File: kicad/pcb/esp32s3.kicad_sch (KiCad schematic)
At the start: 7 parts, among them SW1 SW_Push, U3 ESP32-S3-WROOM-2, Y1 Crystal_GND23

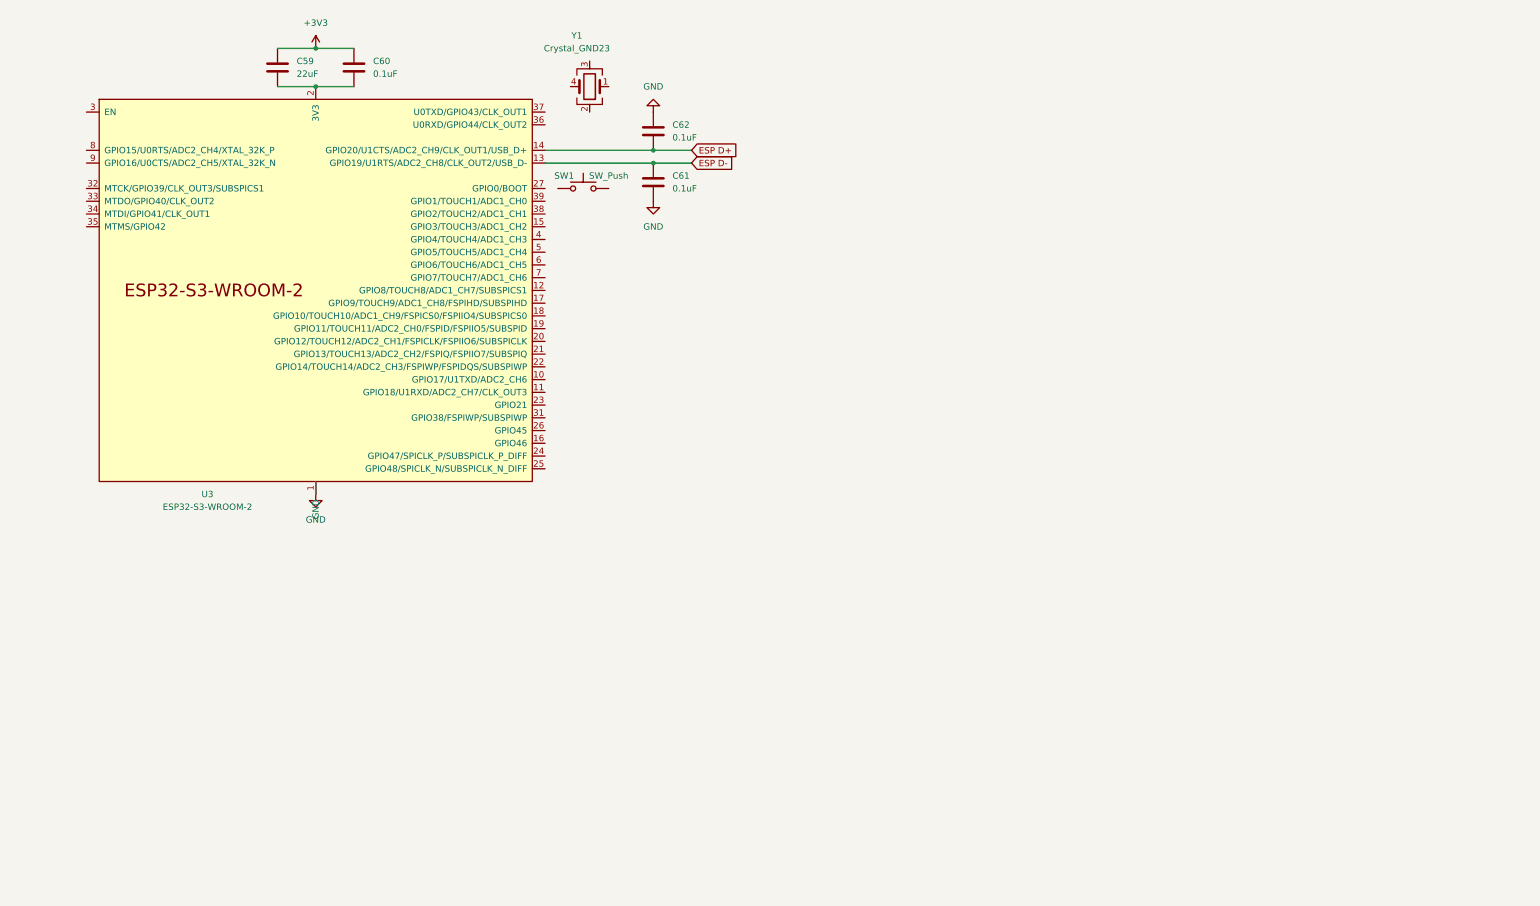
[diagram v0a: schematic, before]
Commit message: USB (almost) done + some STM progress
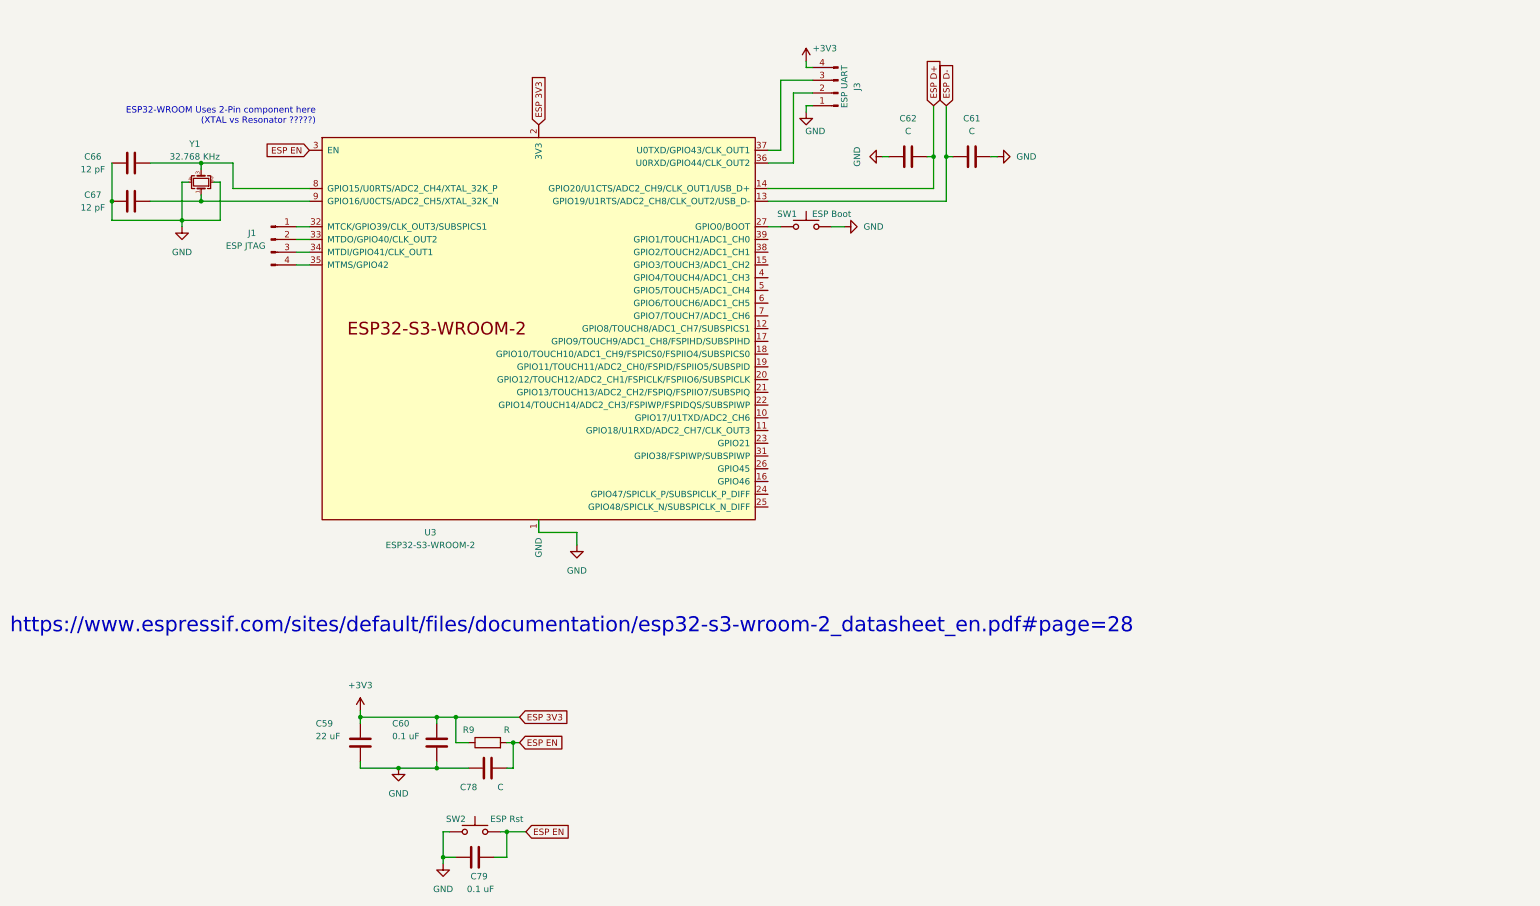
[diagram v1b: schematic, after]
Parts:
- removed Y1: Crystal_GND23, symbol Device:Crystal_GND23
- added C66, C67: 12 pF, symbol Device:C
- added C78: C, symbol Device:C
- added C79: 0.1 uF, symbol Device:C
- added J1: ESP JTAG, symbol Connector:Conn_01x04_Pin
- added J3: ESP UART, symbol Connector:Conn_01x04_Pin
- added R9: R, symbol Device:R
- added SW2: ESP Rst, symbol Switch:SW_Push
- added Y1: 32.768 KHz, symbol Device:Crystal_GND24_Small
- C59: value 22uF -> 22 uF
- C60: value 0.1uF -> 0.1 uF
- C61, C62: value 0.1uF -> C
- SW1: value SW_Push -> ESP Boot
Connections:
- net +3V3: now also U3.2 (3V3), J3.4 (Pin_4), R9.1
- net GND: now also C59.2, C60.2, SW1.2, C66.1, C67.2, C78.1, C79.1, J3.1 (Pin_1), SW2.1, Y1.2, Y1.4
- net at SW1.1: now also U3.27 (GPIO0/BOOT)
- net ESP EN: now reaches U3.3 (EN)
- net ESP EN: now also C78.2, C79.2, R9.2, SW2.2
- net at U3.32 (MTCK/GPIO39/CLK_OUT3/SUBSPICS1): now also J1.1 (Pin_1)
- net at U3.33 (MTDO/GPIO40/CLK_OUT2): now also J1.2 (Pin_2)
- net at U3.34 (MTDI/GPIO41/CLK_OUT1): now also J1.3 (Pin_3)
- net at U3.35 (MTMS/GPIO42): now also J1.4 (Pin_4)
- net at U3.36 (U0RXD/GPIO44/CLK_OUT2): now also J3.2 (Pin_2)
- net at U3.37 (U0TXD/GPIO43/CLK_OUT1): now also J3.3 (Pin_3)
- net at U3.8 (GPIO15/U0RTS/ADC2_CH4/XTAL_32K_P): now also C66.2, Y1.3
- net at U3.9 (GPIO16/U0CTS/ADC2_CH5/XTAL_32K_N): now also C67.1, Y1.1
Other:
- note added: "ESP32-WROOM Uses 2-Pin component here (XTAL vs Resonator ?????)"
- note added: "https://www.espressif.com/sites/default/files/documentation/esp32-s3-wroom-2_datasheet_en.pdf#page=28"
- moved on the sheet: C61, C62, SW1, U3

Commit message: Initial support circuitry for STM and ESP
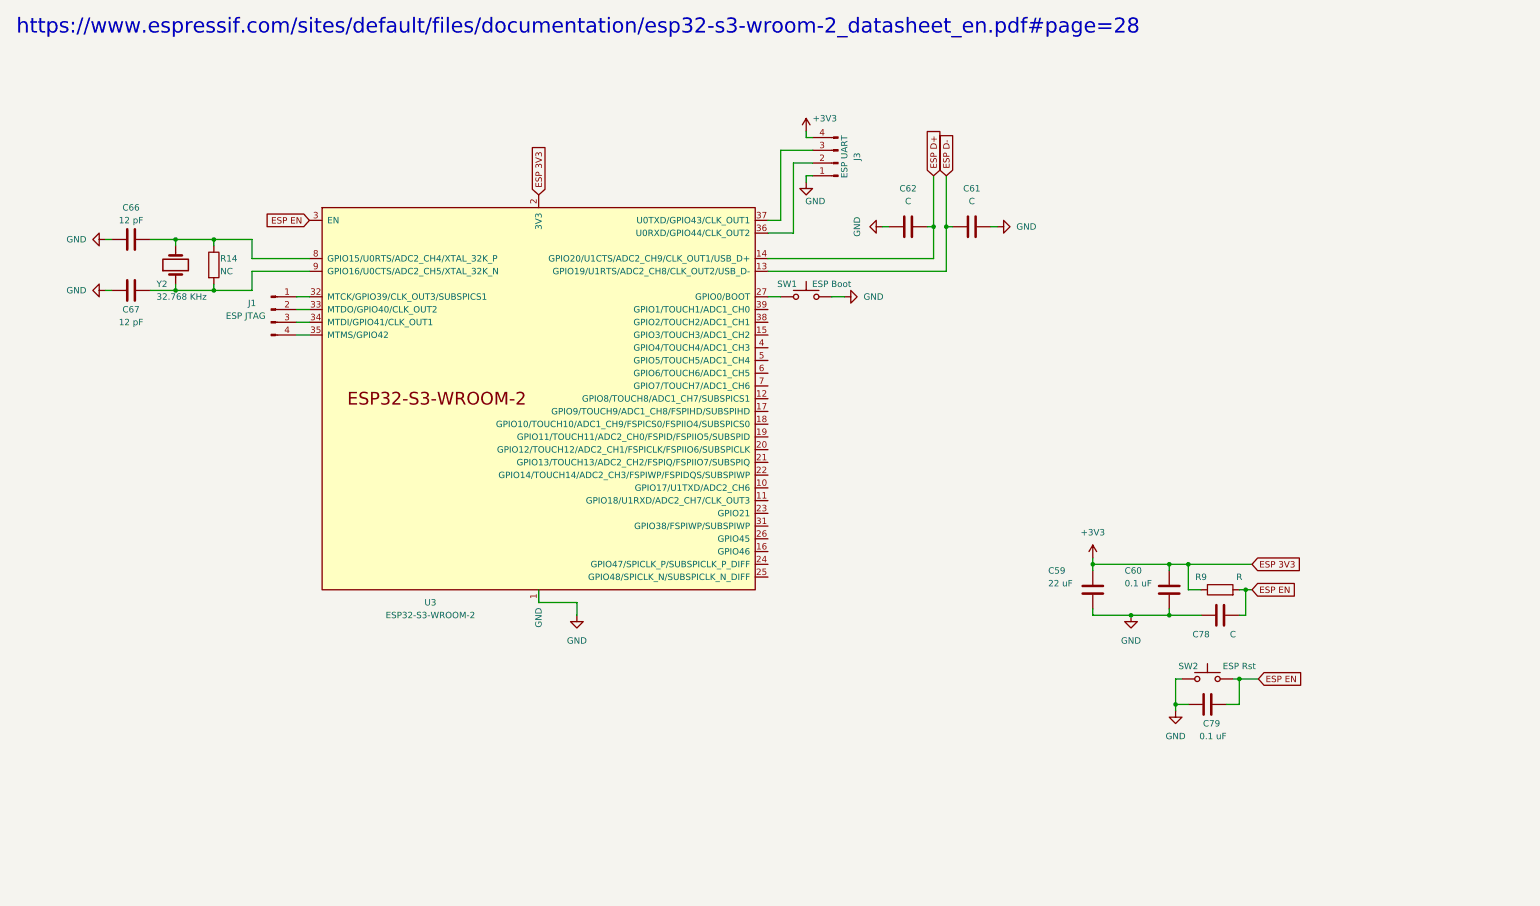
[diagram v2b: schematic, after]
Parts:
- removed Y1: 32.768 KHz, symbol Device:Crystal_GND24_Small
- added R14: NC, symbol Device:R
- added Y2: 32.768 KHz, symbol Device:Crystal
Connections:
- net at C67.1, U3.9 (GPIO16/U0CTS/ADC2_CH5/XTAL_32K_N): now also R14.2, Y2.1
- net at C66.2, U3.8 (GPIO15/U0RTS/ADC2_CH4/XTAL_32K_P): now also R14.1, Y2.2
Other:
- note removed: "ESP32-WROOM Uses 2-Pin component here (XTAL vs Resonator ?????)"
- moved on the sheet: C59, C60, C61, C62, C66, C67, C78, C79, J1, J3, R9, SW1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

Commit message: Initial wiring sorted out?
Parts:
- removed J1: ESP JTAG, symbol Connector:Conn_01x04_Pin
- removed J3: ESP UART, symbol Connector:Conn_01x04_Pin
- added J1: ESP JTAG, symbol Connector_Generic:Conn_01x04
- added J3: ESP UART, symbol Connector_Generic:Conn_01x04
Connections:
- net +3V3: now also J3.1 (Pin_1)
- net GND: now also J3.4 (Pin_4)
- net at U3.36 (U0RXD/GPIO44/CLK_OUT2): now also J3.3 (Pin_3)
- net at U3.37 (U0TXD/GPIO43/CLK_OUT1): now also J3.2 (Pin_2)
- net at U3.32 (MTCK/GPIO39/CLK_OUT3/SUBSPICS1): now also J1.4 (Pin_4)
- net at U3.33 (MTDO/GPIO40/CLK_OUT2): now also J1.3 (Pin_3)
- net at U3.34 (MTDI/GPIO41/CLK_OUT1): now also J1.2 (Pin_2)
- net at U3.35 (MTMS/GPIO42): now also J1.1 (Pin_1)
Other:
- moved on the sheet: C61, C62, C66, C67, R14, SW1, U3, Y2

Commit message: Hub wired(?) + STM and ESP may boot already
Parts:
- C59: value 22 uF -> 22u; footprint (none) -> Capacitor_SMD:C_0402_1005Metric_Pad0.74x0.62mm_HandSolder
- C60, C79: value 0.1 uF -> 0.1u; footprint (none) -> Capacitor_SMD:C_0402_1005Metric_Pad0.74x0.62mm_HandSolder
- C61, C62, C78: footprint (none) -> Capacitor_SMD:C_0402_1005Metric_Pad0.74x0.62mm_HandSolder
- C66, C67: value 12 pF -> 12p; footprint (none) -> Capacitor_SMD:C_0402_1005Metric_Pad0.74x0.62mm_HandSolder
- J1, J3: footprint (none) -> Connector_PinHeader_2.54mm:PinHeader_1x04_P2.54mm_Vertical_SMD_Pin1Right
- R14, R9: footprint (none) -> Resistor_SMD:R_0402_1005Metric_Pad0.72x0.64mm_HandSolder
- SW1, SW2: footprint (none) -> Button_Switch_SMD:SW_Push_1P1T_NO_CK_KMR2
- Y2: footprint (none) -> Crystal:Crystal_SMD_2012-2Pin_2.0x1.2mm
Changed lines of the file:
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@@
   (junction (at 266.7 129.54) (diameter 0) (color 0 0 0 0)
   )
-  (junction (at 255.27 124.46) (diameter 0) (color 0 0 0 0)
-  )
   (junction (at 243.84 134.62) (diameter 0) (color 0 0 0 0)
   )
@@
     (stroke (width 0) (type default))
   )
-  (wire (pts (xy 255.27 124.46) (xy 267.97 124.46))
-    (stroke (width 0) (type default))
-  )
   (wire (pts (xy 196.85 55.88) (xy 198.12 55.88))
     (stroke (width 0) (type default))
@@
   )
   (wire (pts (xy 151.13 148.59) (xy 143.51 148.59))
+    (stroke (width 0) (type default))
+  )
+  (wire (pts (xy 143.51 66.04) (xy 143.51 67.31))
     (stroke (width 0) (type default))
   )
@@
     )
   )
-  (global_label "ESP 3V3" (shape input) (at 143.51 67.31 90) (fields_autoplaced)
-    (effects (font (size 1.27 1.27)) (justify left))
-    (property "Intersheetrefs" "${INTERSHEET_REFS}" (at 143.51 56.2211 90)
-      (effects (font (size 1.27 1.27)) (justify left) hide)
-    )
-  )
   (global_label "ESP EN" (shape input) (at 267.97 129.54 0) (fields_autoplaced)
     (effects (font (size 1.27 1.27)) (justify left))
@@
     )
   )
-  (global_label "ESP 3V3" (shape input) (at 267.97 124.46 0) (fields_autoplaced)
-    (effects (font (size 1.27 1.27)) (justify left))
-    (property "Intersheetrefs" "${INTERSHEET_REFS}" (at 279.0589 124.46 0)
-      (effects (font (size 1.27 1.27)) (justify left) hide)
-    )
-  )
   (global_label "ESP D-" (shape input) (at 224.79 63.5 90) (fields_autoplaced)
     (effects (font (size 1.27 1.27)) (justify left))
@@
       (effects (font (size 1.27 1.27)) (justify left))
     )
-    (property "Footprint" "" (at 203.2 58.42 0)
+    (property "Footprint" "Connector_PinHeader_2.54mm:PinHeader_1x04_P2.54mm_Vertical_SMD_Pin1Right" (at 203.2 58.42 0)
       (effects (font (size 1.27 1.27)) hide)
     )
@@
       (effects (font (size 1.27 1.27)))
     )
-    (property "Footprint" "" (at 265.43 133.6548 0)
+    (property "Footprint" "Capacitor_SMD:C_0402_1005Metric_Pad0.74x0.62mm_HandSolder" (at 265.43 133.6548 0)
       (effects (font (size 1.27 1.27)) hide)
     )
@@
       (effects (font (size 1.27 1.27)))
     )
-    (property "Footprint" "" (at 196.85 82.55 0)
+    (property "Footprint" "Button_Switch_SMD:SW_Push_1P1T_NO_CK_KMR2" (at 196.85 82.55 0)
       (effects (font (size 1.27 1.27)) hide)
     )
@@
       (effects (font (size 1.27 1.27)) (justify right))
     )
-    (property "Footprint" "" (at 71.12 81.28 0)
+    (property "Footprint" "Crystal:Crystal_SMD_2012-2Pin_2.0x1.2mm" (at 71.12 81.28 0)
       (effects (font (size 1.27 1.27)) hide)
     )
@@
       (effects (font (size 1.27 1.27)))
     )
-    (property "Footprint" "" (at 261.62 131.318 90)
+    (property "Footprint" "Resistor_SMD:R_0402_1005Metric_Pad0.72x0.64mm_HandSolder" (at 261.62 131.318 90)
       (effects (font (size 1.27 1.27)) hide)
     )
@@
       (effects (font (size 1.27 1.27)) (justify left))
     )
-    (property "Value" "0.1 uF" (at 242.57 128.27 0)
-      (effects (font (size 1.27 1.27)) (justify left))
-    )
-    (property "Footprint" "" (at 252.4252 133.35 0)
+    (property "Value" "0.1u" (at 242.57 128.27 0)
+      (effects (font (size 1.27 1.27)) (justify left))
+    )
+    (property "Footprint" "Capacitor_SMD:C_0402_1005Metric_Pad0.74x0.62mm_HandSolder" (at 252.4252 133.35 0)
       (effects (font (size 1.27 1.27)) hide)
     )
@@
       (effects (font (size 1.27 1.27)))
     )
-    (property "Footprint" "" (at 213.36 74.6252 0)
+    (property "Footprint" "Capacitor_SMD:C_0402_1005Metric_Pad0.74x0.62mm_HandSolder" (at 213.36 74.6252 0)
       (effects (font (size 1.27 1.27)) hide)
     )
@@
       (effects (font (size 1.27 1.27)) (justify left))
     )
-    (property "Value" "22 uF" (at 227.33 128.27 0)
-      (effects (font (size 1.27 1.27)) (justify left))
-    )
-    (property "Footprint" "" (at 237.1852 133.35 0)
+    (property "Value" "22u" (at 227.33 128.27 0)
+      (effects (font (size 1.27 1.27)) (justify left))
+    )
+    (property "Footprint" "Capacitor_SMD:C_0402_1005Metric_Pad0.74x0.62mm_HandSolder" (at 237.1852 133.35 0)
       (effects (font (size 1.27 1.27)) hide)
     )
@@
       (effects (font (size 1.27 1.27)))
     )
-    (property "Footprint" "" (at 226.06 74.6252 0)
+    (property "Footprint" "Capacitor_SMD:C_0402_1005Metric_Pad0.74x0.62mm_HandSolder" (at 226.06 74.6252 0)
       (effects (font (size 1.27 1.27)) hide)
     )
@@
       (effects (font (size 1.27 1.27)))
     )
-    (property "Value" "12 pF" (at 62.23 92.71 90)
-      (effects (font (size 1.27 1.27)))
-    )
-    (property "Footprint" "" (at 58.42 87.3252 0)
+    (property "Value" "12p" (at 62.23 92.71 90)
+      (effects (font (size 1.27 1.27)))
+    )
+    (property "Footprint" "Capacitor_SMD:C_0402_1005Metric_Pad0.74x0.62mm_HandSolder" (at 58.42 87.3252 0)
       (effects (font (size 1.27 1.27)) hide)
     )
@@
       (effects (font (size 1.27 1.27)))
     )
-    (property "Footprint" "" (at 90.17 92.71 0)
+    (property "Footprint" "Connector_PinHeader_2.54mm:PinHeader_1x04_P2.54mm_Vertical_SMD_Pin1Right" (at 90.17 92.71 0)
       (effects (font (size 1.27 1.27)) hide)
     )
@@
       (effects (font (size 1.27 1.27)))
     )
-    (property "Footprint" "" (at 259.08 142.24 0)
+    (property "Footprint" "Button_Switch_SMD:SW_Push_1P1T_NO_CK_KMR2" (at 259.08 142.24 0)
       (effects (font (size 1.27 1.27)) hide)
     )
@@
       (effects (font (size 1.27 1.27)) (justify left))
     )
-    (property "Footprint" "" (at 76.962 81.28 90)
+    (property "Footprint" "Resistor_SMD:R_0402_1005Metric_Pad0.72x0.64mm_HandSolder" (at 76.962 81.28 90)
       (effects (font (size 1.27 1.27)) hide)
     )
@@
       (effects (font (size 1.27 1.27)) (justify left))
     )
-    (property "Value" "0.1 uF" (at 262.89 158.75 90)
-      (effects (font (size 1.27 1.27)) (justify left))
-    )
-    (property "Footprint" "" (at 262.89 151.4348 0)
+    (property "Value" "0.1u" (at 262.89 158.75 90)
+      (effects (font (size 1.27 1.27)) (justify left))
+    )
+    (property "Footprint" "Capacitor_SMD:C_0402_1005Metric_Pad0.74x0.62mm_HandSolder" (at 262.89 151.4348 0)
       (effects (font (size 1.27 1.27)) hide)
     )
@@
     )
   )
+  (symbol (lib_id "power:+3V3") (at 143.51 66.04 0) (unit 1)
+    (in_bom yes) (on_board yes) (dnp no) (fields_autoplaced)
+    (property "Reference" "#PWR066" (at 143.51 69.85 0)
+      (effects (font (size 1.27 1.27)) hide)
+    )
+    (property "Value" "+3V3" (at 143.51 60.96 0)
+      (effects (font (size 1.27 1.27)))
+    )
+    (property "Footprint" "" (at 143.51 66.04 0)
+      (effects (font (size 1.27 1.27)) hide)
+    )
+    (property "Datasheet" "" (at 143.51 66.04 0)
+      (effects (font (size 1.27 1.27)) hide)
+    )
+    (pin "1")
+    (instances
+      (project "pcb"
+        (path "/3c00b562-f31c-4144-9978-9a1bbba7ab3a/0692a0a8-8e1d-4cc2-ba10-8dd4a1e1097a"
+          (reference "#PWR066") (unit 1)
+        )
+      )
+    )
+  )
   (symbol (lib_id "Device:C") (at 62.23 76.2 90) (unit 1)
     (in_bom yes) (on_board yes) (dnp no)
@@
       (effects (font (size 1.27 1.27)))
     )
-    (property "Value" "12 pF" (at 62.23 72.39 90)
-      (effects (font (size 1.27 1.27)))
-    )
-    (property "Footprint" "" (at 66.04 75.2348 0)
-      (effects (font (size 1.27 1.27)) hide)
-    )
+    (property "Value" "12p" (at 62.23 72.39 90)
+      (effects (font (size 1.27 1.27)))
+    )
+    (property "Footprint" "Capacitor_SMD:C_0402_1005Metric_Pad0.74x0.62mm_HandSolder" (at 66.04 75.2348 0)
+      (effects (font (size 1.27 1.27)) hide)
+    )

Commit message: (WIP) Tracing v2
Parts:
- removed C61, C62: C, Capacitor_SMD:C_0402_1005Metric_Pad0.74x0.62mm_HandSolder, symbol Device:C
- removed R14: NC, Resistor_SMD:R_0402_1005Metric_Pad0.72x0.64mm_HandSolder, symbol Device:R
- added J6: LS0XX, Connector_FFC-FPC:Molex_54548-1071_1x10-1MP_P0.5mm_Horizontal, symbol Connector:Conn_01x10_Pin
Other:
- moved on the sheet: C66, C67, Y2
